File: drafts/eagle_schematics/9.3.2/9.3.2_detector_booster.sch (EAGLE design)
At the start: 17 parts, among them IC1 LMV393D, Q1 CSD88539ND, Q2 CSD88539ND, Q3 2N7002

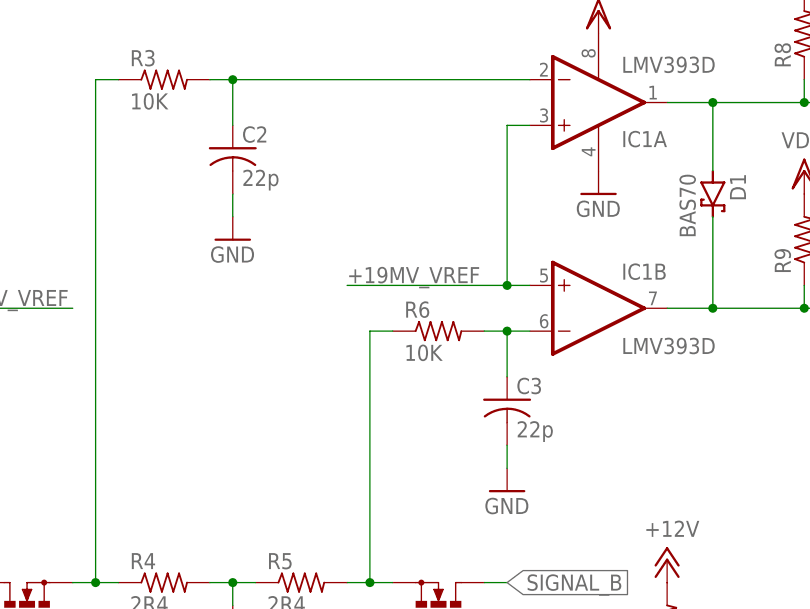
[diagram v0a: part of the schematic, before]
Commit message: Update RailCom reference circuits.
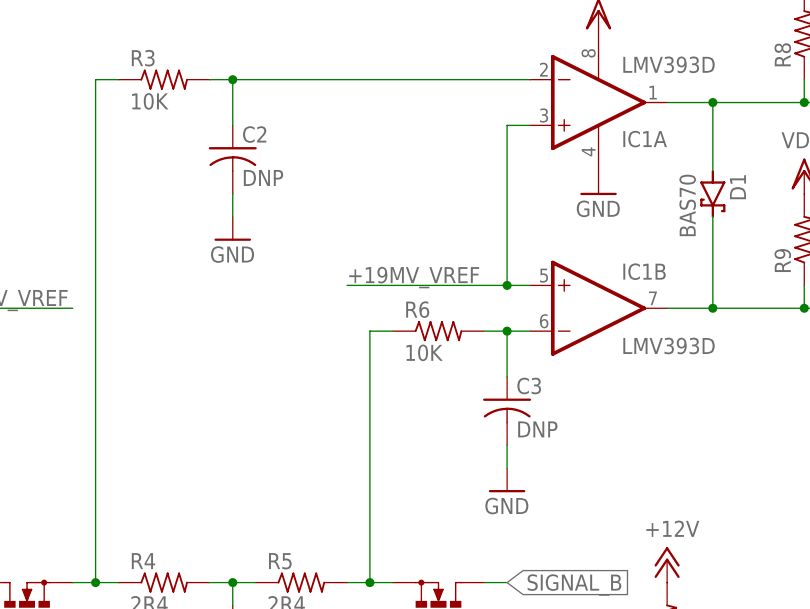
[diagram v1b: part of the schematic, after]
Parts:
- C2, C3: value 22p -> DNP
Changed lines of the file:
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@@
 <part name="R5" library="resistor" library_urn="urn:adsk.eagle:library:348" deviceset="R-US_" device="R1206" package3d_urn="urn:adsk.eagle:package:26062/1" value="2R4"/>
 <part name="R3" library="resistor" library_urn="urn:adsk.eagle:library:348" deviceset="R-US_" device="R0402" package3d_urn="urn:adsk.eagle:package:26058/1" value="10K"/>
-<part name="C2" library="rcl" library_urn="urn:adsk.eagle:library:334" deviceset="C-US" device="C0402" package3d_urn="urn:adsk.eagle:package:23626/2" value="22p"/>
+<part name="C2" library="rcl" library_urn="urn:adsk.eagle:library:334" deviceset="C-US" device="C0402" package3d_urn="urn:adsk.eagle:package:23626/2" value="DNP"/>
 <part name="P+1" library="supply1" library_urn="urn:adsk.eagle:library:371" deviceset="+12V" device=""/>
 <part name="Q3" library="transistor-power" library_urn="urn:adsk.eagle:library:400" deviceset="IRF512" device="" package3d_urn="urn:adsk.eagle:package:29484/3" value="2N7002"/>
@@
 <part name="R8" library="resistor" library_urn="urn:adsk.eagle:library:348" deviceset="R-US_" device="R0402" package3d_urn="urn:adsk.eagle:package:26058/1" value="2K4"/>
 <part name="VDD2" library="supply1" library_urn="urn:adsk.eagle:library:371" deviceset="VDD" device=""/>
-<part name="C3" library="rcl" library_urn="urn:adsk.eagle:library:334" deviceset="C-US" device="C0402" package3d_urn="urn:adsk.eagle:package:23626/2" value="22p"/>
+<part name="C3" library="rcl" library_urn="urn:adsk.eagle:library:334" deviceset="C-US" device="C0402" package3d_urn="urn:adsk.eagle:package:23626/2" value="DNP"/>
 <part name="R6" library="resistor" library_urn="urn:adsk.eagle:library:348" deviceset="R-US_" device="R0402" package3d_urn="urn:adsk.eagle:package:26058/1" value="10K"/>
 <part name="GND5" library="supply1" library_urn="urn:adsk.eagle:library:371" deviceset="GND" device=""/>
